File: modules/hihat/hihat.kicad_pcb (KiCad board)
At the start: 2 copper layers, 30.5 x 68.6 mm, 4 parts

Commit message: Started basic pcb layout
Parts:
- added C1: 100pf, Capacitor_SMD:C_0402_1005Metric, F.Cu at (56.6, 57.5)
- added C2: 1nf, Capacitor_SMD:C_0402_1005Metric, F.Cu at (59.3, 63.5)
- added C3: 1nf, Capacitor_SMD:C_0402_1005Metric, F.Cu at (62.4, 63.5)
- added C4: 0.1uf, Capacitor_SMD:C_0402_1005Metric, F.Cu at (122.2, 81.2)
- added C5: 0.1uf, Capacitor_SMD:C_0402_1005Metric, F.Cu at (122.2, 83.1)
- added C6: 47uf, Capacitor_SMD:C_0805_2012Metric, F.Cu at (61.5, 61.1)
- added C7: 10nf, Capacitor_SMD:C_0402_1005Metric, F.Cu at (122.2, 85.1)
- added C8: 4.7uf, Capacitor_SMD:C_0603_1608Metric, F.Cu at (119.2, 92.5)
- added D1: SS8050, Package_TO_SOT_SMD:SOT-23, F.Cu at (119.6, 61.9)
- added D2: SS14, Diode_SMD:D_SMA, F.Cu at (113.2, 90.5)
- added D3: SS8050, Package_TO_SOT_SMD:SOT-23, F.Cu at (119.6, 66.5)
- added D4: SS8550, Package_TO_SOT_SMD:SOT-23, F.Cu at (119.6, 71.1)
- added R1: 330, Resistor_SMD:R_0402_1005Metric, F.Cu at (59.3, 66.2)
- added R10: 10k, Resistor_SMD:R_0402_1005Metric, F.Cu at (67.8, 60.1)
- added R11: 1k, Resistor_SMD:R_0402_1005Metric, F.Cu at (62.4, 66.2)
- added R12: 330, Resistor_SMD:R_0402_1005Metric, F.Cu at (113.5, 83.2)
- added R13: 100k, Resistor_SMD:R_0402_1005Metric, F.Cu at (113.5, 85.2)
- added R14: 22k, Resistor_SMD:R_0402_1005Metric, F.Cu at (113.5, 87.2)
- added R15: 330, Resistor_SMD:R_0402_1005Metric, F.Cu at (116.4, 75.3)
- added R16: 10k, Resistor_SMD:R_0402_1005Metric, F.Cu at (116.4, 77.2)
- added R17: 100k, Resistor_SMD:R_0402_1005Metric, F.Cu at (116.4, 79.2)
- added R18: 100k, Resistor_SMD:R_0402_1005Metric, F.Cu at (116.4, 81.2)
- added R19: 10k, Resistor_SMD:R_0402_1005Metric, F.Cu at (116.4, 83.2)
- added R2: 100k, Resistor_SMD:R_0402_1005Metric, F.Cu at (56.6, 60.1)
- added R20: 200k, Resistor_SMD:R_0402_1005Metric, F.Cu at (116.4, 85.2)
- added R21: 100k, Resistor_SMD:R_0402_1005Metric, F.Cu at (116.4, 87.2)
- added R22: 1M, Resistor_SMD:R_0402_1005Metric, F.Cu at (119.3, 75.3)
- added R23: 1M, Resistor_SMD:R_0402_1005Metric, F.Cu at (119.3, 77.2)
- added R24: 100k, Resistor_SMD:R_0402_1005Metric, F.Cu at (119.3, 79.2)
- added R25: 1k, Resistor_SMD:R_0402_1005Metric, F.Cu at (119.3, 81.2)
- added R3: 1k, Resistor_SMD:R_0402_1005Metric, F.Cu at (67.8, 55.1)
- added R4: 200k, Resistor_SMD:R_0402_1005Metric, F.Cu at (56.6, 55.2)
- added R5: 330, Resistor_SMD:R_0402_1005Metric, F.Cu at (65.5, 63.5)
- added R6: 330, Resistor_SMD:R_0402_1005Metric, F.Cu at (65.5, 66.2)
- added R7: 1k, Resistor_SMD:R_0402_1005Metric, F.Cu at (110.6, 87.2)
- added R8: 1k, Resistor_SMD:R_0402_1005Metric, F.Cu at (113.5, 75.3)
- added R9: 22k, Resistor_SMD:R_0402_1005Metric, F.Cu at (67.8, 57.5)
- added RV1: 50k, BreadModular_Pots:Potentiometer_RV09, F.Cu at (54.7, 73.0)
- added RV2: 50k, BreadModular_Pots:Potentiometer_RV09, F.Cu at (70.0, 73.0)
- added U1: VTL5C, BreadModular_MISC:VTL5C, B.Cu at (62.6, 64.9)
- added U2: MCP6002-xSN, Package_SO:SOIC-8-1EP_3.9x4.9mm_P1.27mm_EP2.29x3mm, F.Cu at (62.3, 57.3)
- added U3: MCP6002-xSN, Package_SO:SOIC-8-1EP_3.9x4.9mm_P1.27mm_EP2.29x3mm, F.Cu at (93.7, 84.2)
- added U4: MCP6002-xSN, Package_SO:SOIC-8-1EP_3.9x4.9mm_P1.27mm_EP2.29x3mm, F.Cu at (93.7, 90.8)
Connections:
- INPUT1 pad 1: unconnected-(INPUT1-Pin_1-Pad1) -> NOISE_IN
- INPUT1 pad 2: unconnected-(INPUT1-Pin_2-Pad2) -> GATE_IN
- INPUT1 pad 3: unconnected-(INPUT1-Pin_3-Pad3) -> CV_ACCENT
- INPUT1 pad 4: unconnected-(INPUT1-Pin_4-Pad4) -> GATE_OPEN
- OUTPUT1 pad 1: unconnected-(OUTPUT1-Pin_1-Pad1) -> HIHAT_OUT
- OUTPUT1 pad 2: unconnected-(OUTPUT1-Pin_2-Pad2) -> HIHAT_OUT
- OUTPUT1 pad 3: unconnected-(OUTPUT1-Pin_3-Pad3) -> HIHAT_OUT
- OUTPUT1 pad 4: unconnected-(OUTPUT1-Pin_4-Pad4) -> CV_OUT
- OUTPUT1 pad 5: unconnected-(OUTPUT1-Pin_5-Pad5) -> CV_OUT
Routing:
- net Net-(R11-Pad1): track 0.00 -> 17.9 mm
- net NOISE_IN: track 0.00 -> 14.0 mm
- net FILTERED_NOISE: track 0.00 -> 13.9 mm
- net Net-(U2A--): track 0.00 -> 13.9 mm
- net HIHAT_OUT: track 0.00 -> 12.2 mm
- net V_MID: track 0.00 -> 9.34 mm, vias 0 -> 3
- net Net-(U2B-+): track 0.00 -> 7.51 mm
- net Net-(U2B--): track 0.00 -> 6.01 mm
- net Net-(R3-Pad1): track 0.00 -> 6.01 mm
- net Net-(C2-Pad2): track 0.00 -> 5.15 mm
- net GND: track 10.2 -> 14.6 mm, vias 0 -> 2
- net Net-(C1-Pad2): track 0.00 -> 2.96 mm
- net Net-(U1--): track 0.00 -> 2.53 mm
- net V_SUPPLY: track 10.2 -> 11.6 mm, vias 0 -> 1
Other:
- board text added: "AC"
- board text added: "AUDIO"
- board text added: "CUTOFF"
- board text added: "CV"
- board text added: "DECAY"
- board text added: "GATE"
- board text added: "HIHAT"
- board text added: "HIHAT 0.1.0"
- board text added: "NOISE"
- board text added: "OPEN"
- board text removed: "NAME"
- board text removed: "NAME 0.0.0"

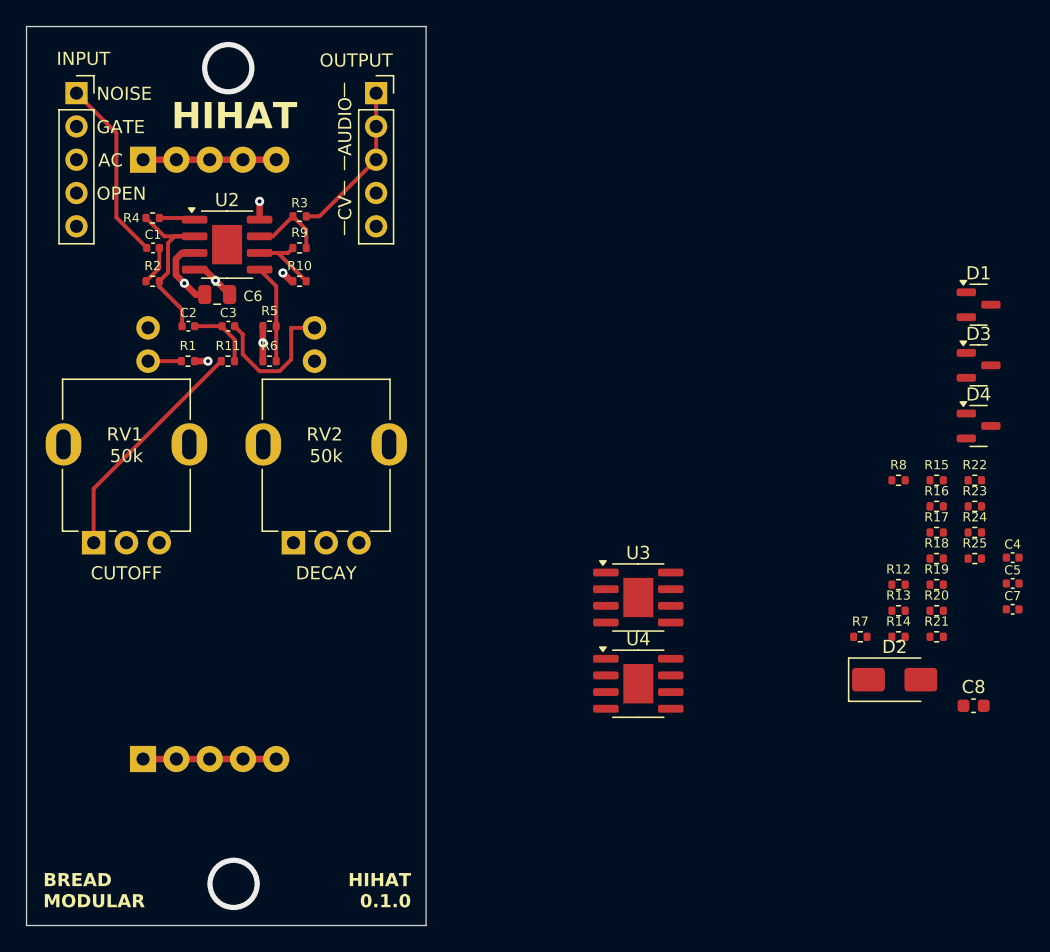
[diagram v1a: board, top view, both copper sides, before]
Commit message: Complete CPU routing
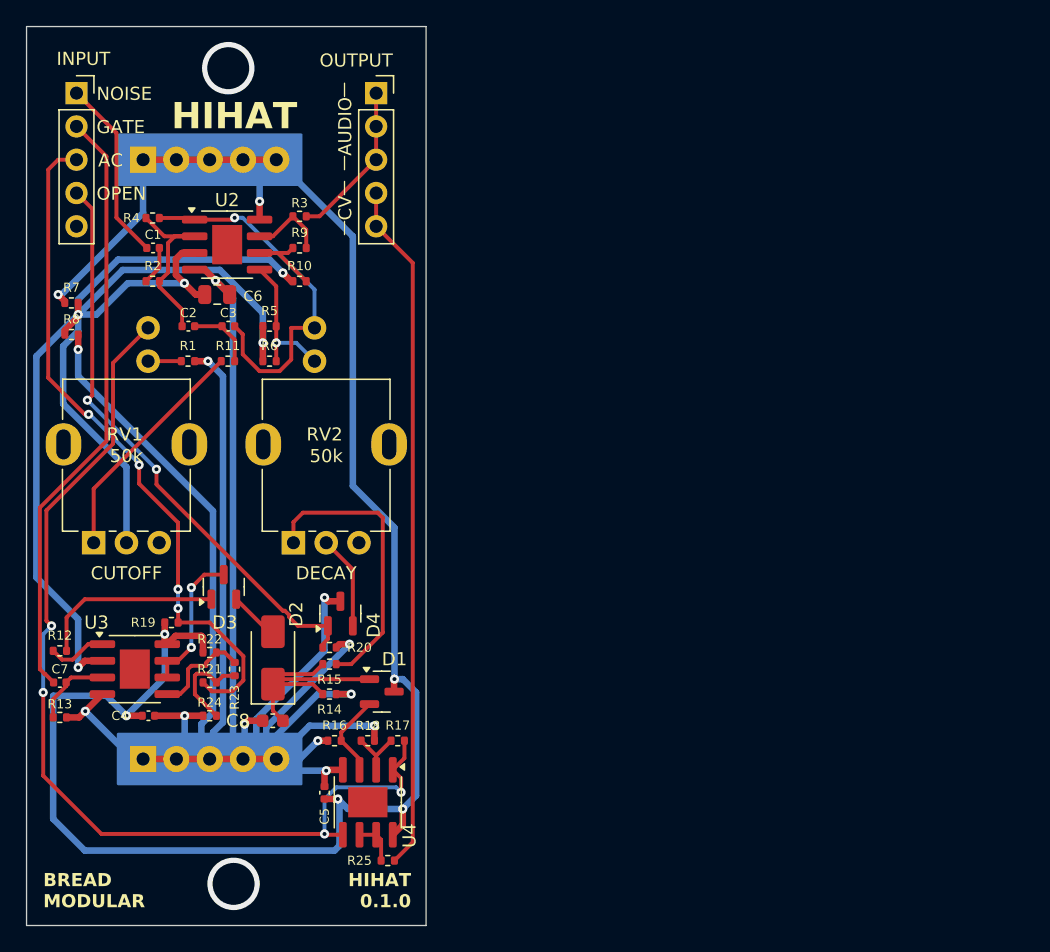
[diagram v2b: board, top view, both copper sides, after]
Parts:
- moved C7 72.9 mm to (49.5, 90.7)
- moved C4 67.0 mm to (56.3, 93.2), turned to 180 degrees
- moved R7 65.4 mm to (50.4, 61.7)
- moved R13 64.5 mm to (49.5, 93.3), turned to 180 degrees
- moved R12 64.2 mm to (49.5, 88.3)
- moved R8 64.1 mm to (50.4, 64.1)
- moved R24 60.0 mm to (61.0, 93.2)
- moved D3 60.0 mm to (62.0, 83.4), turned to 90 degrees
- moved R22 59.8 mm to (61.0, 88.4), turned to 180 degrees
- moved R19 58.4 mm to (58.0, 86.1), turned to 180 degrees
- moved R23 57.8 mm to (62.9, 89.7), turned to 90 degrees
- moved R21 55.6 mm to (61.0, 90.7), turned to 180 degrees
- moved C5 54.9 mm to (69.7, 99.1), turned to -90 degrees
- moved D1 54.3 mm to (74.1, 91.4)
- moved C8 53.5 mm to (65.8, 93.6)
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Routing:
- net GND: track 14.6 -> 201.9 mm, vias 2 -> 12
- net V_SUPPLY: track 11.6 -> 150.3 mm, vias 1 -> 7
- net V_MID: track 9.34 -> 110.4 mm, vias 3 -> 5
- net TRANSIENT_CV: track 0.00 -> 76.1 mm, vias 0 -> 4
- net CV_ACCENT: track 0.00 -> 52.9 mm, vias 0 -> 4
- net CV_OUT: track 0.00 -> 52.7 mm
- net GATE_IN: track 0.00 -> 45.9 mm
- net GATE_OPEN: track 0.00 -> 44.3 mm, vias 0 -> 2
- net Net-(R15-Pad1): track 0.00 -> 22.2 mm
- net Net-(D2-K): track 0.00 -> 19.2 mm
- net FILTERED_NOISE: track 13.9 -> 28.3 mm, vias 0 -> 1
- net Net-(D3-K-Pad1): track 0.00 -> 14.2 mm
- net Net-(D3-A): track 0.00 -> 11.0 mm, vias 0 -> 2
- net Net-(U3B-+): track 0.00 -> 7.68 mm
- net Net-(R21-Pad1): track 0.00 -> 7.32 mm
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
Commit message: hihat: Add MIDI support Now we don't need seperate cables for GATE, Accent & Open Hat. We can control all these via a single MIDI cable.
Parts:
- added C9: 100uf, Capacitor_SMD:C_1206_3216Metric, F.Cu at (57.0, 100.8)
- added R26: 4.7k, Resistor_SMD:R_0402_1005Metric, F.Cu at (62.2, 101.0)
- added R27: 10k, Resistor_SMD:R_0402_1005Metric, F.Cu at (50.3, 96.8)
- added U5: ATtiny1616-M, Package_DFN_QFN:VQFN-20-1EP_3x3mm_P0.4mm_EP1.7x1.7mm, F.Cu at (51.7, 100.6)
- added V_SUPPLY2: Conn_01x05_Pin, BreadModular_MISC:Conn_Holes_2, B.Cu at (66.9, 101.1)
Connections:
- INPUT1 pad 2: GATE_IN -> MIDI
- INPUT1 pad 3: CV_ACCENT -> GATE_IN
- INPUT1 pad 4: GATE_OPEN -> CV_ACCENT
- INPUT1 pad 5: unconnected-(INPUT1-Pin_5-Pad5) -> GATE_OPEN
- R19 pad 2: V_SUPPLY -> MIDI_VELOCITY
- R20 pad 1: GND -> MIDI_OPEN
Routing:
- net MIDI: track 0.00 -> 53.9 mm
- net MIDI_OPEN: track 0.00 -> 30.2 mm, vias 0 -> 2
- net MIDI_VELOCITY: track 0.00 -> 21.5 mm, vias 0 -> 2
- net TX: track 0.00 -> 20.8 mm
- net V_SUPPLY: track 150.3 -> 165.1 mm, vias 7 -> 8
- net Net-(U5-~{RESET}/PA0): track 0.00 -> 11.2 mm
- net TRANSIENT_CV: track 76.1 -> 81.1 mm
- net GATE_IN: track 45.9 -> 50.9 mm
- net MIDI_GATE: track 0.00 -> 4.38 mm, vias 0 -> 2
- net CV_ACCENT: track 52.9 -> 50.1 mm
- net UDPI: track 0.00 -> 2.42 mm
- net GATE_OPEN: track 44.3 -> 42.1 mm
- net GND: track 201.9 -> 200.6 mm
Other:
- board text added: "GT"
- board text added: "HIHAT 0.2.0"
- board text added: "MIDI"
- board text added: "OP"
- board text added: "TX"
- board text added: "U"
- board text removed: "GATE"
- board text removed: "HIHAT 0.1.0"
- board text removed: "OPEN"
